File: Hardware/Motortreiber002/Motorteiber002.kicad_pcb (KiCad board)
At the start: 2 copper layers, 159.8 x 99.8 mm, 0 parts

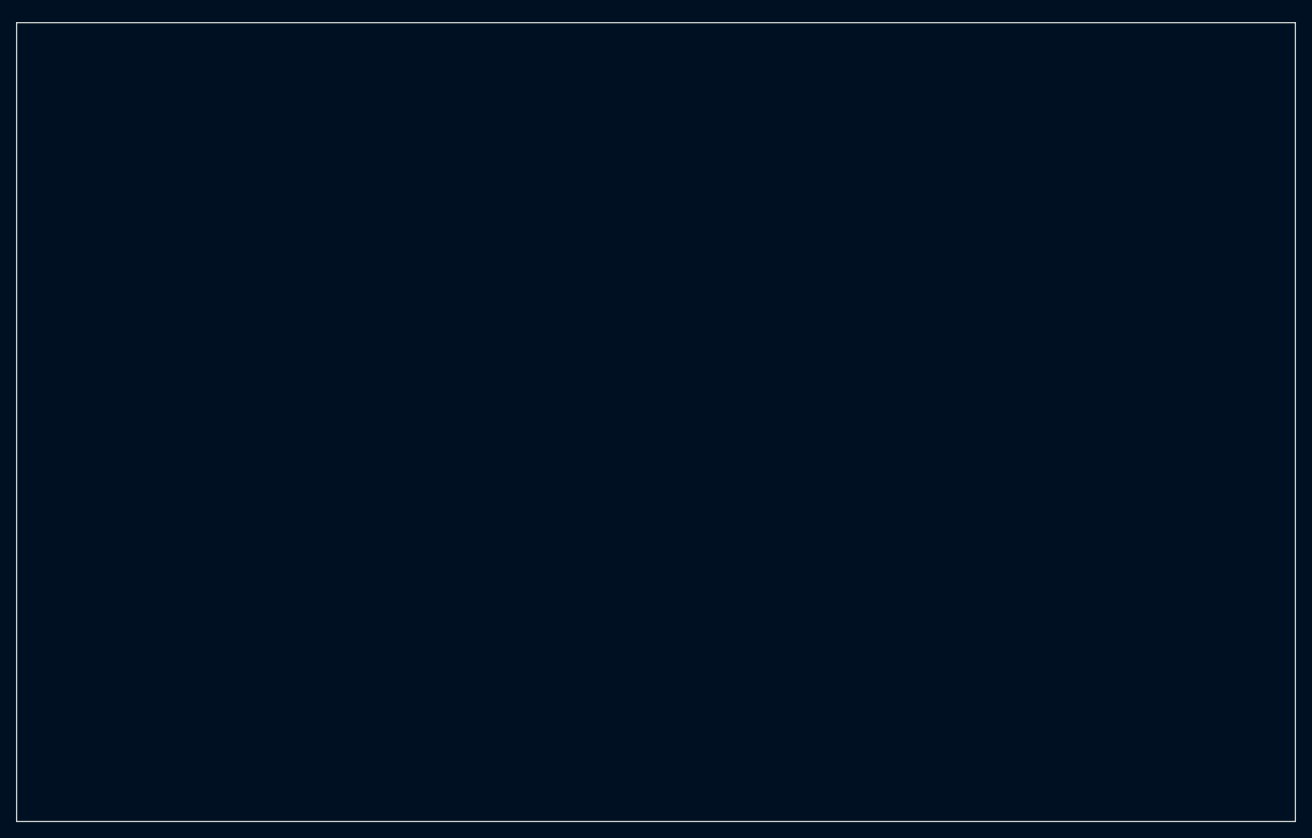
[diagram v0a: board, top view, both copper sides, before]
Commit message: Mega64 hinzu
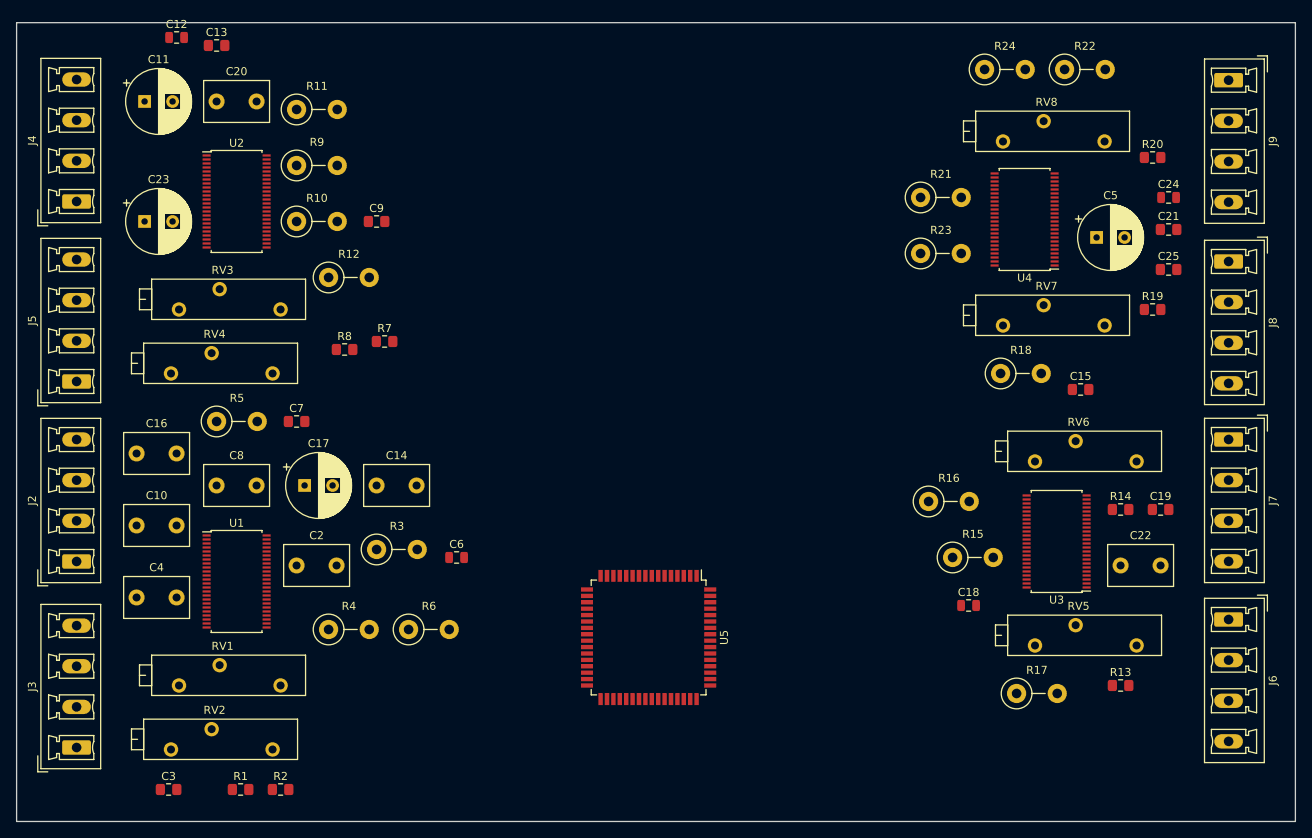
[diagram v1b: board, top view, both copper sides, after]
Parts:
- added C10: 100nF, Capacitor_THT:C_Disc_D8.0mm_W5.0mm_P5.00mm, F.Cu at (70.0, 108.0)
- added C11: 100uF, Capacitor_THT:CP_Radial_D8.0mm_P3.50mm, F.Cu at (71.0, 55.0)
- added C12: 10nF, Capacitor_SMD:C_0805_2012Metric, F.Cu at (75.0, 47.0)
- added C13: 100nf, Capacitor_SMD:C_0805_2012Metric_Pad1.15x1.40mm_HandSolder, F.Cu at (80.0, 48.0)
- added C14: 100nF, Capacitor_THT:C_Disc_D8.0mm_W5.0mm_P5.00mm, F.Cu at (100.0, 103.0)
- added C15: 100nF, Capacitor_SMD:C_0805_2012Metric_Pad1.15x1.40mm_HandSolder, F.Cu at (188.0, 91.0)
- added C16: 100nF, Capacitor_THT:C_Disc_D8.0mm_W5.0mm_P5.00mm, F.Cu at (70.0, 99.0)
- added C17: 100uF, Capacitor_THT:CP_Radial_D8.0mm_P3.50mm, F.Cu at (91.0, 103.0)
- added C18: 10nF, Capacitor_SMD:C_0805_2012Metric, F.Cu at (174.0, 118.0)
- added C19: 100nf, Capacitor_SMD:C_0805_2012Metric_Pad1.15x1.40mm_HandSolder, F.Cu at (198.0, 106.0)
- added C2: 100nF, Capacitor_THT:C_Disc_D8.0mm_W5.0mm_P5.00mm, F.Cu at (90.0, 113.0)
- added C20: 100nF, Capacitor_THT:C_Disc_D8.0mm_W5.0mm_P5.00mm, F.Cu at (80.0, 55.0)
- added C21: 100nF, Capacitor_SMD:C_0805_2012Metric_Pad1.15x1.40mm_HandSolder, F.Cu at (199.0, 71.0)
- added C22: 100nF, Capacitor_THT:C_Disc_D8.0mm_W5.0mm_P5.00mm, F.Cu at (193.0, 113.0)
- added C23: 100uF, Capacitor_THT:CP_Radial_D8.0mm_P3.50mm, F.Cu at (71.0, 70.0)
- added C24: 10nF, Capacitor_SMD:C_0805_2012Metric, F.Cu at (199.0, 67.0)
- added C25: 100nf, Capacitor_SMD:C_0805_2012Metric_Pad1.15x1.40mm_HandSolder, F.Cu at (199.0, 76.0)
- added C3: 100nF, Capacitor_SMD:C_0805_2012Metric_Pad1.15x1.40mm_HandSolder, F.Cu at (74.0, 141.0)
- added C4: 100nF, Capacitor_THT:C_Disc_D8.0mm_W5.0mm_P5.00mm, F.Cu at (70.0, 117.0)
- added C5: 100uF, Capacitor_THT:CP_Radial_D8.0mm_P3.50mm, F.Cu at (190.0, 72.0)
- added C6: 10nF, Capacitor_SMD:C_0805_2012Metric, F.Cu at (110.0, 112.0)
- added C7: 100nf, Capacitor_SMD:C_0805_2012Metric_Pad1.15x1.40mm_HandSolder, F.Cu at (90.0, 95.0)
- added C8: 100nF, Capacitor_THT:C_Disc_D8.0mm_W5.0mm_P5.00mm, F.Cu at (80.0, 103.0)
- added C9: 100nF, Capacitor_SMD:C_0805_2012Metric_Pad1.15x1.40mm_HandSolder, F.Cu at (100.0, 70.0)
- added J2: Screw_Terminal_01x04, Connector_Phoenix_MC_HighVoltage:PhoenixContact_MCV_1,5_4-G-5.08_1x04_P5.08mm_Vertical, F.Cu at (62.5, 112.5)
- added J3: Screw_Terminal_01x04, Connector_Phoenix_MC_HighVoltage:PhoenixContact_MCV_1,5_4-G-5.08_1x04_P5.08mm_Vertical, F.Cu at (62.5, 135.8)
- added J4: Screw_Terminal_01x04, Connector_Phoenix_MC_HighVoltage:PhoenixContact_MCV_1,5_4-G-5.08_1x04_P5.08mm_Vertical, F.Cu at (62.5, 67.5)
- added J5: Screw_Terminal_01x04, Connector_Phoenix_MC_HighVoltage:PhoenixContact_MCV_1,5_4-G-5.08_1x04_P5.08mm_Vertical, F.Cu at (62.5, 90.0)
- added J6: Screw_Terminal_01x04, Connector_Phoenix_MC_HighVoltage:PhoenixContact_MCV_1,5_4-G-5.08_1x04_P5.08mm_Vertical, F.Cu at (206.5, 119.8)
- added J7: Screw_Terminal_01x04, Connector_Phoenix_MC_HighVoltage:PhoenixContact_MCV_1,5_4-G-5.08_1x04_P5.08mm_Vertical, F.Cu at (206.5, 97.2)
- added J8: Screw_Terminal_01x04, Connector_Phoenix_MC_HighVoltage:PhoenixContact_MCV_1,5_4-G-5.08_1x04_P5.08mm_Vertical, F.Cu at (206.5, 75.0)
- added J9: Screw_Terminal_01x04, Connector_Phoenix_MC_HighVoltage:PhoenixContact_MCV_1,5_4-G-5.08_1x04_P5.08mm_Vertical, F.Cu at (206.5, 52.3)
- added R1: R, Resistor_SMD:R_0805_2012Metric_Pad1.15x1.40mm_HandSolder, F.Cu at (83.0, 141.0)
- added R10: 0R5, Resistor_THT:R_Axial_DIN0411_L9.9mm_D3.6mm_P5.08mm_Vertical, F.Cu at (90.0, 70.0)
- added R11: 0R5, Resistor_THT:R_Axial_DIN0411_L9.9mm_D3.6mm_P5.08mm_Vertical, F.Cu at (90.0, 56.0)
- added R12: 0R5, Resistor_THT:R_Axial_DIN0411_L9.9mm_D3.6mm_P5.08mm_Vertical, F.Cu at (94.0, 77.0)
- added R13: R, Resistor_SMD:R_0805_2012Metric_Pad1.15x1.40mm_HandSolder, F.Cu at (193.0, 128.0)
- added R14: R, Resistor_SMD:R_0805_2012Metric_Pad1.15x1.40mm_HandSolder, F.Cu at (193.0, 106.0)
- added R15: 0R5, Resistor_THT:R_Axial_DIN0411_L9.9mm_D3.6mm_P5.08mm_Vertical, F.Cu at (172.0, 112.0)
- added R16: 0R5, Resistor_THT:R_Axial_DIN0411_L9.9mm_D3.6mm_P5.08mm_Vertical, F.Cu at (169.0, 105.0)
- added R17: 0R5, Resistor_THT:R_Axial_DIN0411_L9.9mm_D3.6mm_P5.08mm_Vertical, F.Cu at (180.0, 129.0)
- added R18: 0R5, Resistor_THT:R_Axial_DIN0411_L9.9mm_D3.6mm_P5.08mm_Vertical, F.Cu at (178.0, 89.0)
- added R19: R, Resistor_SMD:R_0805_2012Metric_Pad1.15x1.40mm_HandSolder, F.Cu at (197.0, 81.0)
- added R2: R, Resistor_SMD:R_0805_2012Metric_Pad1.15x1.40mm_HandSolder, F.Cu at (88.0, 141.0)
- added R20: R, Resistor_SMD:R_0805_2012Metric_Pad1.15x1.40mm_HandSolder, F.Cu at (197.0, 62.0)
- added R21: 0R5, Resistor_THT:R_Axial_DIN0411_L9.9mm_D3.6mm_P5.08mm_Vertical, F.Cu at (168.0, 67.0)
- added R22: 0R5, Resistor_THT:R_Axial_DIN0411_L9.9mm_D3.6mm_P5.08mm_Vertical, F.Cu at (186.0, 51.0)
- added R23: 0R5, Resistor_THT:R_Axial_DIN0411_L9.9mm_D3.6mm_P5.08mm_Vertical, F.Cu at (168.0, 74.0)
- added R24: 0R5, Resistor_THT:R_Axial_DIN0411_L9.9mm_D3.6mm_P5.08mm_Vertical, F.Cu at (176.0, 51.0)
- added R3: 0R5, Resistor_THT:R_Axial_DIN0411_L9.9mm_D3.6mm_P5.08mm_Vertical, F.Cu at (100.0, 111.0)
- added R4: 0R5, Resistor_THT:R_Axial_DIN0411_L9.9mm_D3.6mm_P5.08mm_Vertical, F.Cu at (94.0, 121.0)
- added R5: 0R5, Resistor_THT:R_Axial_DIN0411_L9.9mm_D3.6mm_P5.08mm_Vertical, F.Cu at (80.0, 95.0)
- added R6: 0R5, Resistor_THT:R_Axial_DIN0411_L9.9mm_D3.6mm_P5.08mm_Vertical, F.Cu at (104.0, 121.0)
- added R7: R, Resistor_SMD:R_0805_2012Metric_Pad1.15x1.40mm_HandSolder, F.Cu at (101.0, 85.0)
- added R8: R, Resistor_SMD:R_0805_2012Metric_Pad1.15x1.40mm_HandSolder, F.Cu at (96.0, 86.0)
- added R9: 0R5, Resistor_THT:R_Axial_DIN0411_L9.9mm_D3.6mm_P5.08mm_Vertical, F.Cu at (90.0, 63.0)
- added RV1: R_POT_TRIM, Potentiometer_THT:Potentiometer_Vishay_43_Horizontal, F.Cu at (88.0, 128.0)
- added RV2: R_POT_TRIM, Potentiometer_THT:Potentiometer_Vishay_43_Horizontal, F.Cu at (87.0, 136.0)
- added RV3: R_POT_TRIM, Potentiometer_THT:Potentiometer_Vishay_43_Horizontal, F.Cu at (88.0, 81.0)
- added RV4: R_POT_TRIM, Potentiometer_THT:Potentiometer_Vishay_43_Horizontal, F.Cu at (87.0, 89.0)
- added RV5: R_POT_TRIM, Potentiometer_THT:Potentiometer_Vishay_43_Horizontal, F.Cu at (195.0, 123.0)
- added RV6: R_POT_TRIM, Potentiometer_THT:Potentiometer_Vishay_43_Horizontal, F.Cu at (195.0, 100.0)
- added RV7: R_POT_TRIM, Potentiometer_THT:Potentiometer_Vishay_43_Horizontal, F.Cu at (191.0, 83.0)
- added RV8: R_POT_TRIM, Potentiometer_THT:Potentiometer_Vishay_43_Horizontal, F.Cu at (191.0, 60.0)
- added U1: DRV8823, Package_SO:TSSOP-48_6.1x12.5mm_P0.5mm, F.Cu at (82.5, 115.0)
- added U2: DRV8823, Package_SO:TSSOP-48_6.1x12.5mm_P0.5mm, F.Cu at (82.5, 67.5)
- added U3: DRV8823, Package_SO:TSSOP-48_6.1x12.5mm_P0.5mm, F.Cu at (185.0, 110.0)
- added U4: DRV8823, Package_SO:TSSOP-48_6.1x12.5mm_P0.5mm, F.Cu at (181.0, 69.8)
- added U5: ATmega64-16AU, Package_QFP:TQFP-64_14x14mm_P0.8mm, F.Cu at (134.0, 122.0)

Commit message: 16 Motortreiber 1 ATXMega 128 mit USB USB Anschluss noch nicht fertig
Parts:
- removed R1, R13, R14, R19, R2, R20, R7, R8: R, Resistor_SMD:R_0805_2012Metric_Pad1.15x1.40mm_HandSolder
- removed RV1, RV2, RV3, RV4, RV5, RV6, RV7, RV8: R_POT_TRIM, Potentiometer_THT:Potentiometer_Vishay_43_Horizontal
- added C26: 100nF, Capacitor_THT:C_Disc_D8.0mm_W5.0mm_P5.00mm, F.Cu at (179.8, -133.7)
- added C27: 100nF, Capacitor_SMD:C_0805_2012Metric_Pad1.15x1.40mm_HandSolder, F.Cu at (189.4, -135.5)
- added C28: 100nF, Capacitor_THT:C_Disc_D8.0mm_W5.0mm_P5.00mm, F.Cu at (179.5, -127.1)
- added C29: 100uF, Capacitor_THT:CP_Radial_D8.0mm_P3.50mm, F.Cu at (170.7, -128.3)
- added C30: 10nF, Capacitor_SMD:C_0805_2012Metric, F.Cu at (189.4, -145.8)
- added C31: 100nf, Capacitor_SMD:C_0805_2012Metric_Pad1.15x1.40mm_HandSolder, F.Cu at (189.4, -132.5)
- added C32: 100nF, Capacitor_THT:C_Disc_D8.0mm_W5.0mm_P5.00mm, F.Cu at (129.7, -97.8)
- added C33: 100nF, Capacitor_SMD:C_0805_2012Metric_Pad1.15x1.40mm_HandSolder, F.Cu at (139.7, -103.2)
- added C34: 100nF, Capacitor_THT:C_Disc_D8.0mm_W5.0mm_P5.00mm, F.Cu at (130.0, -104.3)
- added C35: 100uF, Capacitor_THT:CP_Radial_D8.0mm_P3.50mm, F.Cu at (120.9, -99.0)
- added C36: 10nF, Capacitor_SMD:C_0805_2012Metric, F.Cu at (139.6, -116.4)
- added C37: 100nf, Capacitor_SMD:C_0805_2012Metric_Pad1.15x1.40mm_HandSolder, F.Cu at (139.7, -106.1)
- added C38: 100nF, Capacitor_THT:C_Disc_D8.0mm_W5.0mm_P5.00mm, F.Cu at (79.9, -68.5)
- added C39: 100nF, Capacitor_SMD:C_0805_2012Metric_Pad1.15x1.40mm_HandSolder, F.Cu at (89.8, -73.8)
- added C40: 100nF, Capacitor_THT:C_Disc_D8.0mm_W5.0mm_P5.00mm, F.Cu at (80.2, -75.0)
- added C41: 100uF, Capacitor_THT:CP_Radial_D8.0mm_P3.50mm, F.Cu at (71.1, -69.7)
- added C42: 10nF, Capacitor_SMD:C_0805_2012Metric, F.Cu at (89.8, -87.1)
- added C43: 100nf, Capacitor_SMD:C_0805_2012Metric_Pad1.15x1.40mm_HandSolder, F.Cu at (89.8, -76.8)
- added C44: 100nF, Capacitor_THT:C_Disc_D8.0mm_W5.0mm_P5.00mm, F.Cu at (30.1, -156.4)
- added C45: 100nF, Capacitor_SMD:C_0805_2012Metric_Pad1.15x1.40mm_HandSolder, F.Cu at (40.0, -164.8)
- added C46: 100nF, Capacitor_THT:C_Disc_D8.0mm_W5.0mm_P5.00mm, F.Cu at (30.4, -163.0)
- added C47: 100uF, Capacitor_THT:CP_Radial_D8.0mm_P3.50mm, F.Cu at (21.3, -157.6)
- added C48: 10nF, Capacitor_SMD:C_0805_2012Metric, F.Cu at (40.0, -175.1)
- added C49: 100nf, Capacitor_SMD:C_0805_2012Metric_Pad1.15x1.40mm_HandSolder, F.Cu at (40.0, -161.8)
- added C50: 100nF, Capacitor_THT:C_Disc_D8.0mm_W5.0mm_P5.00mm, F.Cu at (130.0, -133.7)
- added C51: 100nF, Capacitor_SMD:C_0805_2012Metric_Pad1.15x1.40mm_HandSolder, F.Cu at (139.7, -132.5)
- added C52: 100nF, Capacitor_THT:C_Disc_D8.0mm_W5.0mm_P5.00mm, F.Cu at (129.7, -127.1)
- added C53: 100uF, Capacitor_THT:CP_Radial_D8.0mm_P3.50mm, F.Cu at (120.9, -128.3)
- added C54: 10nF, Capacitor_SMD:C_0805_2012Metric, F.Cu at (139.6, -145.8)
- added C55: 100nf, Capacitor_SMD:C_0805_2012Metric_Pad1.15x1.40mm_HandSolder, F.Cu at (139.7, -135.5)
- added C56: 100nF, Capacitor_THT:C_Disc_D8.0mm_W5.0mm_P5.00mm, F.Cu at (79.9, -97.8)
- added C57: 100nF, Capacitor_SMD:C_0805_2012Metric_Pad1.15x1.40mm_HandSolder, F.Cu at (89.8, -103.2)
- added C58: 100nF, Capacitor_THT:C_Disc_D8.0mm_W5.0mm_P5.00mm, F.Cu at (80.2, -104.3)
- added C59: 100uF, Capacitor_THT:CP_Radial_D8.0mm_P3.50mm, F.Cu at (71.1, -99.0)
- added C60: 10nF, Capacitor_SMD:C_0805_2012Metric, F.Cu at (89.8, -116.4)
- added C61: 100nf, Capacitor_SMD:C_0805_2012Metric_Pad1.15x1.40mm_HandSolder, F.Cu at (89.8, -106.1)
- added C62: 100nF, Capacitor_THT:C_Disc_D8.0mm_W5.0mm_P5.00mm, F.Cu at (30.1, -68.5)
- added C63: 100nF, Capacitor_SMD:C_0805_2012Metric_Pad1.15x1.40mm_HandSolder, F.Cu at (40.0, -73.8)
- added C64: 100nF, Capacitor_THT:C_Disc_D8.0mm_W5.0mm_P5.00mm, F.Cu at (30.4, -75.0)
- added C65: 100uF, Capacitor_THT:CP_Radial_D8.0mm_P3.50mm, F.Cu at (21.3, -69.7)
- added C66: 10nF, Capacitor_SMD:C_0805_2012Metric, F.Cu at (40.0, -87.1)
- added C67: 100nf, Capacitor_SMD:C_0805_2012Metric_Pad1.15x1.40mm_HandSolder, F.Cu at (40.0, -76.8)
- added C68: 100nF, Capacitor_THT:C_Disc_D8.0mm_W5.0mm_P5.00mm, F.Cu at (130.0, -163.0)
- added C69: 100nF, Capacitor_SMD:C_0805_2012Metric_Pad1.15x1.40mm_HandSolder, F.Cu at (139.7, -164.8)
- added C70: 100nF, Capacitor_THT:C_Disc_D8.0mm_W5.0mm_P5.00mm, F.Cu at (129.7, -156.4)
- added C71: 100uF, Capacitor_THT:CP_Radial_D8.0mm_P3.50mm, F.Cu at (120.9, -157.6)
- added C72: 10nF, Capacitor_SMD:C_0805_2012Metric, F.Cu at (139.6, -175.1)
- added C73: 100nf, Capacitor_SMD:C_0805_2012Metric_Pad1.15x1.40mm_HandSolder, F.Cu at (139.7, -161.8)
- added C74: 100nF, Capacitor_THT:C_Disc_D8.0mm_W5.0mm_P5.00mm, F.Cu at (80.2, -133.7)
- added C75: 100nF, Capacitor_SMD:C_0805_2012Metric_Pad1.15x1.40mm_HandSolder, F.Cu at (89.8, -132.5)
- added C76: 100nF, Capacitor_THT:C_Disc_D8.0mm_W5.0mm_P5.00mm, F.Cu at (79.9, -127.1)
- added C77: 100uF, Capacitor_THT:CP_Radial_D8.0mm_P3.50mm, F.Cu at (71.1, -128.3)
- added C78: 10nF, Capacitor_SMD:C_0805_2012Metric, F.Cu at (89.8, -145.8)
- added C79: 100nf, Capacitor_SMD:C_0805_2012Metric_Pad1.15x1.40mm_HandSolder, F.Cu at (89.8, -135.5)
- added C80: 100nF, Capacitor_THT:C_Disc_D8.0mm_W5.0mm_P5.00mm, F.Cu at (30.4, -104.3)
- added C81: 100nF, Capacitor_SMD:C_0805_2012Metric_Pad1.15x1.40mm_HandSolder, F.Cu at (40.0, -106.1)
- added C82: 100nF, Capacitor_THT:C_Disc_D8.0mm_W5.0mm_P5.00mm, F.Cu at (30.1, -97.8)
- added C83: 100uF, Capacitor_THT:CP_Radial_D8.0mm_P3.50mm, F.Cu at (21.3, -99.0)
- added C84: 10nF, Capacitor_SMD:C_0805_2012Metric, F.Cu at (40.0, -116.4)
- added C85: 100nf, Capacitor_SMD:C_0805_2012Metric_Pad1.15x1.40mm_HandSolder, F.Cu at (40.0, -103.2)
- added C86: 100nF, Capacitor_THT:C_Disc_D8.0mm_W5.0mm_P5.00mm, F.Cu at (79.9, -156.4)
- added C87: 100nF, Capacitor_SMD:C_0805_2012Metric_Pad1.15x1.40mm_HandSolder, F.Cu at (89.8, -161.8)
- added C88: 100nF, Capacitor_THT:C_Disc_D8.0mm_W5.0mm_P5.00mm, F.Cu at (80.2, -163.0)
- added C89: 100uF, Capacitor_THT:CP_Radial_D8.0mm_P3.50mm, F.Cu at (71.1, -157.6)
- added C90: 10nF, Capacitor_SMD:C_0805_2012Metric, F.Cu at (89.8, -175.1)
- added C91: 100nf, Capacitor_SMD:C_0805_2012Metric_Pad1.15x1.40mm_HandSolder, F.Cu at (89.8, -164.8)
- added C92: 100nF, Capacitor_THT:C_Disc_D8.0mm_W5.0mm_P5.00mm, F.Cu at (30.4, -133.7)
- added C93: 100nF, Capacitor_SMD:C_0805_2012Metric_Pad1.15x1.40mm_HandSolder, F.Cu at (40.0, -135.5)
- added C94: 100nF, Capacitor_THT:C_Disc_D8.0mm_W5.0mm_P5.00mm, F.Cu at (30.1, -127.1)
- added C95: 100uF, Capacitor_THT:CP_Radial_D8.0mm_P3.50mm, F.Cu at (21.3, -128.3)
- added C96: 10nF, Capacitor_SMD:C_0805_2012Metric, F.Cu at (40.0, -145.8)
- added C97: 100nf, Capacitor_SMD:C_0805_2012Metric_Pad1.15x1.40mm_HandSolder, F.Cu at (40.0, -132.5)
- added J10: Screw_Terminal_01x04, Connector_Phoenix_MC_HighVoltage:PhoenixContact_MCV_1,5_4-G-5.08_1x04_P5.08mm_Vertical, F.Cu at (148.7, -141.8)
- added J11: Screw_Terminal_01x04, Connector_Phoenix_MC_HighVoltage:PhoenixContact_MCV_1,5_4-G-5.08_1x04_P5.08mm_Vertical, F.Cu at (148.7, -132.5)
- added J12: Screw_Terminal_01x04, Connector_Phoenix_MC_HighVoltage:PhoenixContact_MCV_1,5_4-G-5.08_1x04_P5.08mm_Vertical, F.Cu at (98.9, -112.5)
- added J13: Screw_Terminal_01x04, Connector_Phoenix_MC_HighVoltage:PhoenixContact_MCV_1,5_4-G-5.08_1x04_P5.08mm_Vertical, F.Cu at (98.9, -103.2)
- added J14: Screw_Terminal_01x04, Connector_Phoenix_MC_HighVoltage:PhoenixContact_MCV_1,5_4-G-5.08_1x04_P5.08mm_Vertical, F.Cu at (49.1, -83.2)
- added J15: Screw_Terminal_01x04, Connector_Phoenix_MC_HighVoltage:PhoenixContact_MCV_1,5_4-G-5.08_1x04_P5.08mm_Vertical, F.Cu at (49.1, -73.8)
- added J16: Screw_Terminal_01x04, Connector_Phoenix_MC_HighVoltage:PhoenixContact_MCV_1,5_4-G-5.08_1x04_P5.08mm_Vertical, F.Cu at (-0.72, -171.2)
- added J17: Screw_Terminal_01x04, Connector_Phoenix_MC_HighVoltage:PhoenixContact_MCV_1,5_4-G-5.08_1x04_P5.08mm_Vertical, F.Cu at (-0.72, -161.8)
- added J18: Screw_Terminal_01x04, Connector_Phoenix_MC_HighVoltage:PhoenixContact_MCV_1,5_4-G-5.08_1x04_P5.08mm_Vertical, F.Cu at (98.9, -132.5)
- added J19: Screw_Terminal_01x04, Connector_Phoenix_MC_HighVoltage:PhoenixContact_MCV_1,5_4-G-5.08_1x04_P5.08mm_Vertical, F.Cu at (98.9, -141.8)
- added J20: Screw_Terminal_01x04, Connector_Phoenix_MC_HighVoltage:PhoenixContact_MCV_1,5_4-G-5.08_1x04_P5.08mm_Vertical, F.Cu at (49.1, -112.5)
- added J21: Screw_Terminal_01x04, Connector_Phoenix_MC_HighVoltage:PhoenixContact_MCV_1,5_4-G-5.08_1x04_P5.08mm_Vertical, F.Cu at (49.1, -103.2)
- added J22: Screw_Terminal_01x04, Connector_Phoenix_MC_HighVoltage:PhoenixContact_MCV_1,5_4-G-5.08_1x04_P5.08mm_Vertical, F.Cu at (-0.72, -73.8)
- added J23: Screw_Terminal_01x04, Connector_Phoenix_MC_HighVoltage:PhoenixContact_MCV_1,5_4-G-5.08_1x04_P5.08mm_Vertical, F.Cu at (-0.72, -83.2)
- added J24: Screw_Terminal_01x04, Connector_Phoenix_MC_HighVoltage:PhoenixContact_MCV_1,5_4-G-5.08_1x04_P5.08mm_Vertical, F.Cu at (98.9, -171.2)
- added J25: Screw_Terminal_01x04, Connector_Phoenix_MC_HighVoltage:PhoenixContact_MCV_1,5_4-G-5.08_1x04_P5.08mm_Vertical, F.Cu at (98.9, -161.8)
- added J26: Screw_Terminal_01x04, Connector_Phoenix_MC_HighVoltage:PhoenixContact_MCV_1,5_4-G-5.08_1x04_P5.08mm_Vertical, F.Cu at (49.1, -132.5)
- added J27: Screw_Terminal_01x04, Connector_Phoenix_MC_HighVoltage:PhoenixContact_MCV_1,5_4-G-5.08_1x04_P5.08mm_Vertical, F.Cu at (49.1, -141.8)
- added J28: Screw_Terminal_01x04, Connector_Phoenix_MC_HighVoltage:PhoenixContact_MCV_1,5_4-G-5.08_1x04_P5.08mm_Vertical, F.Cu at (-0.72, -103.2)
- added J29: Screw_Terminal_01x04, Connector_Phoenix_MC_HighVoltage:PhoenixContact_MCV_1,5_4-G-5.08_1x04_P5.08mm_Vertical, F.Cu at (-0.72, -112.5)
- added J30: Screw_Terminal_01x04, Connector_Phoenix_MC_HighVoltage:PhoenixContact_MCV_1,5_4-G-5.08_1x04_P5.08mm_Vertical, F.Cu at (49.1, -161.8)
- added J31: Screw_Terminal_01x04, Connector_Phoenix_MC_HighVoltage:PhoenixContact_MCV_1,5_4-G-5.08_1x04_P5.08mm_Vertical, F.Cu at (49.1, -171.2)
- added J32: Screw_Terminal_01x04, Connector_Phoenix_MC_HighVoltage:PhoenixContact_MCV_1,5_4-G-5.08_1x04_P5.08mm_Vertical, F.Cu at (-0.72, -132.5)
- added J33: Screw_Terminal_01x04, Connector_Phoenix_MC_HighVoltage:PhoenixContact_MCV_1,5_4-G-5.08_1x04_P5.08mm_Vertical, F.Cu at (-0.72, -141.8)
- added R27: 0R5, Resistor_THT:R_Axial_DIN0411_L9.9mm_D3.6mm_P5.08mm_Vertical, F.Cu at (147.7, -126.0)
- added R28: 0R5, Resistor_THT:R_Axial_DIN0411_L9.9mm_D3.6mm_P5.08mm_Vertical, F.Cu at (180.1, -139.5)
- added R29: 0R5, Resistor_THT:R_Axial_DIN0411_L9.9mm_D3.6mm_P5.08mm_Vertical, F.Cu at (180.1, -144.7)
- added R30: 0R5, Resistor_THT:R_Axial_DIN0411_L9.9mm_D3.6mm_P5.08mm_Vertical, F.Cu at (157.3, -126.0)
- added R33: 0R5, Resistor_THT:R_Axial_DIN0411_L9.9mm_D3.6mm_P5.08mm_Vertical, F.Cu at (130.3, -110.2)
- added R34: 0R5, Resistor_THT:R_Axial_DIN0411_L9.9mm_D3.6mm_P5.08mm_Vertical, F.Cu at (130.3, -115.3)
- added R35: 0R5, Resistor_THT:R_Axial_DIN0411_L9.9mm_D3.6mm_P5.08mm_Vertical, F.Cu at (97.8, -96.7)
- added R36: 0R5, Resistor_THT:R_Axial_DIN0411_L9.9mm_D3.6mm_P5.08mm_Vertical, F.Cu at (107.5, -96.7)
- added R39: 0R5, Resistor_THT:R_Axial_DIN0411_L9.9mm_D3.6mm_P5.08mm_Vertical, F.Cu at (57.7, -67.3)
- added R40: 0R5, Resistor_THT:R_Axial_DIN0411_L9.9mm_D3.6mm_P5.08mm_Vertical, F.Cu at (48.0, -67.3)
- added R41: 0R5, Resistor_THT:R_Axial_DIN0411_L9.9mm_D3.6mm_P5.08mm_Vertical, F.Cu at (80.5, -86.0)
- added R42: 0R5, Resistor_THT:R_Axial_DIN0411_L9.9mm_D3.6mm_P5.08mm_Vertical, F.Cu at (80.5, -80.8)
- added R45: 0R5, Resistor_THT:R_Axial_DIN0411_L9.9mm_D3.6mm_P5.08mm_Vertical, F.Cu at (30.7, -168.8)
- added R46: 0R5, Resistor_THT:R_Axial_DIN0411_L9.9mm_D3.6mm_P5.08mm_Vertical, F.Cu at (30.7, -174.0)
- added R47: 0R5, Resistor_THT:R_Axial_DIN0411_L9.9mm_D3.6mm_P5.08mm_Vertical, F.Cu at (7.88, -155.3)
- added R48: 0R5, Resistor_THT:R_Axial_DIN0411_L9.9mm_D3.6mm_P5.08mm_Vertical, F.Cu at (-1.75, -155.3)
- added R51: 0R5, Resistor_THT:R_Axial_DIN0411_L9.9mm_D3.6mm_P5.08mm_Vertical, F.Cu at (130.3, -139.5)
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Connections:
- J2 pad 1: /Motortreiber1/MA1 -> /Motortreiber4/MA1
- J2 pad 2: /Motortreiber1/MA2 -> /Motortreiber4/MA2
- J2 pad 3: /Motortreiber1/MB2 -> /Motortreiber4/MB2
- J2 pad 4: /Motortreiber1/MB1 -> /Motortreiber4/MB1
- J3 pad 1: /Motortreiber1/MC1 -> /Motortreiber4/MC1
- J3 pad 2: /Motortreiber1/MC2 -> /Motortreiber4/MC2
- J3 pad 3: /Motortreiber1/MD1 -> /Motortreiber4/MD1
- J3 pad 4: /Motortreiber1/MD2 -> /Motortreiber4/MD2
- J4 pad 1: /Motortreiber2/MA1 -> /Motortreiber5/MA1
- J4 pad 2: /Motortreiber2/MA2 -> /Motortreiber5/MA2
- J4 pad 3: /Motortreiber2/MB2 -> /Motortreiber5/MB2
- J4 pad 4: /Motortreiber2/MB1 -> /Motortreiber5/MB1
- J5 pad 1: /Motortreiber2/MC1 -> /Motortreiber5/MC1
- J5 pad 2: /Motortreiber2/MC2 -> /Motortreiber5/MC2
- J5 pad 3: /Motortreiber2/MD1 -> /Motortreiber5/MD1
- J5 pad 4: /Motortreiber2/MD2 -> /Motortreiber5/MD2
- J8 pad 1: /Motortreiber4/MA1 -> /Motortreiber2/MA1
- J8 pad 2: /Motortreiber4/MA2 -> /Motortreiber2/MA2
- J8 pad 3: /Motortreiber4/MB2 -> /Motortreiber2/MB2
- J8 pad 4: /Motortreiber4/MB1 -> /Motortreiber2/MB1
- J9 pad 1: /Motortreiber4/MC1 -> /Motortreiber2/MC1
- J9 pad 2: /Motortreiber4/MC2 -> /Motortreiber2/MC2
- J9 pad 3: /Motortreiber4/MD1 -> /Motortreiber2/MD1
- J9 pad 4: /Motortreiber4/MD2 -> /Motortreiber2/MD2
- U1 pad 17: Net-(RV1-Pad2) -> /Motortreiber4/ABVRef
- U1 pad 18: Net-(RV2-Pad2) -> /Motortreiber4/CDVRef
- U1 pad 20: /Motortreiber1/MD2 -> /Motortreiber4/MD2
- U1 pad 22: /Motortreiber1/MD1 -> /Motortreiber4/MD1
- U1 pad 25: /Motortreiber1/MC2 -> /Motortreiber4/MC2
- U1 pad 27: /Motortreiber1/MC1 -> /Motortreiber4/MC1
- U1 pad 3: /Motortreiber1/MA2 -> /Motortreiber4/MA2
- U1 pad 30: /Ue1 -> /Strobe4
- U1 pad 45: /CS1 -> /CS
- U1 pad 46: /Motortreiber1/MB1 -> /Motortreiber4/MB1
- U1 pad 48: /Motortreiber1/MB2 -> /Motortreiber4/MB2
- U1 pad 5: /Motortreiber1/MA1 -> /Motortreiber4/MA1
- U2 pad 17: Net-(RV3-Pad2) -> /Motortreiber5/ABVRef
- U2 pad 18: Net-(RV4-Pad2) -> /Motortreiber5/CDVRef
- U2 pad 20: /Motortreiber2/MD2 -> /Motortreiber5/MD2
- U2 pad 22: /Motortreiber2/MD1 -> /Motortreiber5/MD1
- U2 pad 25: /Motortreiber2/MC2 -> /Motortreiber5/MC2
- U2 pad 27: /Motortreiber2/MC1 -> /Motortreiber5/MC1
- U2 pad 3: /Motortreiber2/MA2 -> /Motortreiber5/MA2
- U2 pad 30: /Ue2 -> /Strobe5
- U2 pad 45: /CS2 -> /CS
- U2 pad 46: /Motortreiber2/MB1 -> /Motortreiber5/MB1
- U2 pad 48: /Motortreiber2/MB2 -> /Motortreiber5/MB2
- U2 pad 5: /Motortreiber2/MA1 -> /Motortreiber5/MA1
- U3 pad 17: Net-(RV5-Pad2) -> /Motortreiber3/ABVRef
- U3 pad 18: Net-(RV6-Pad2) -> /Motortreiber3/CDVRef
- U3 pad 30: /Ue3 -> /Strobe3
- U3 pad 45: /CS3 -> /CS
- U4 pad 17: Net-(RV7-Pad2) -> /Motortreiber2/ABVRef
- U4 pad 18: Net-(RV8-Pad2) -> /Motortreiber2/CDVRef
- U4 pad 20: /Motortreiber4/MD2 -> /Motortreiber2/MD2
- U4 pad 22: /Motortreiber4/MD1 -> /Motortreiber2/MD1
- U4 pad 25: /Motortreiber4/MC2 -> /Motortreiber2/MC2
- U4 pad 27: /Motortreiber4/MC1 -> /Motortreiber2/MC1
- U4 pad 3: /Motortreiber4/MA2 -> /Motortreiber2/MA2
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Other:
- board size 159.8 x 99.8 mm -> 210 x 290 mm

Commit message: Annotation auf Seiten bezogen
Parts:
- removed C10, C14, C16, C2, C20, C22, C26, C28, C32, C34, C38, C4, C40, C44, C46, C50, C52, C56, C58, C62, C64, C68, C70, C74, C76, C8, C80, C82, C86, C88, C92, C94: 100nF, Capacitor_THT:C_Disc_D8.0mm_W5.0mm_P5.00mm
- removed C11, C17, C23, C29, C35, C41, C47, C5, C53, C59, C65, C71, C77, C83, C89, C95: 100uF, Capacitor_THT:CP_Radial_D8.0mm_P3.50mm
- removed C12, C18, C24, C30, C36, C42, C48, C54, C6, C60, C66, C72, C78, C84, C90, C96: 10nF, Capacitor_SMD:C_0805_2012Metric
- removed C13, C19, C25, C31, C37, C43, C49, C55, C61, C67, C7, C73, C79, C85, C91, C97: 100nf, Capacitor_SMD:C_0805_2012Metric_Pad1.15x1.40mm_HandSolder
- removed C15, C21, C27, C3, C33, C39, C45, C51, C57, C63, C69, C75, C81, C87, C9, C93: 100nF, Capacitor_SMD:C_0805_2012Metric_Pad1.15x1.40mm_HandSolder
- removed J10, J11, J12, J13, J14, J15, J16, J17, J18, J19, J2, J20, J21, J22, J23, J24, J25, J26, J27, J28, J29, J3, J30, J31, J32, J33, J4, J5, J6, J7, J8, J9: Screw_Terminal_01x04, Connector_Phoenix_MC_HighVoltage:PhoenixContact_MCV_1,5_4-G-5.08_1x04_P5.08mm_Vertical
- removed R10, R11, R12, R15, R16, R17, R18, R21, R22, R23, R24, R27, R28, R29, R3, R30, R33, R34, R35, R36, R39, R4, R40, R41, R42, R45, R46, R47, R48, R5, R51, R52, R53, R54, R57, R58, R59, R6, R60, R63, R64, R65, R66, R69, R70, R71, R72, R75, R76, R77, R78, R81, R82, R83, R84, R87, R88, R89, R9, R90, R93, R94, R95, R96: 0R5, Resistor_THT:R_Axial_DIN0411_L9.9mm_D3.6mm_P5.08mm_Vertical
- removed U1, U10, U11, U12, U13, U14, U15, U16, U17, U18, U2, U3, U4, U7, U8, U9: DRV8823, Package_SO:TSSOP-48_6.1x12.5mm_P0.5mm
- removed U5: ADUM3160, Package_SO:SOIC-16W_7.5x10.3mm_P1.27mm
- removed U6: ATxmega128C3-AU, Package_QFP:TQFP-64_14x14mm_P0.8mm
- added C1001: 100nF, Capacitor_THT:C_Disc_D8.0mm_W5.0mm_P5.00mm, F.Cu at (85.6, -125.7)
- added C1002: 100nF, Capacitor_SMD:C_0805_2012Metric_Pad1.15x1.40mm_HandSolder, F.Cu at (95.6, -131.1)
- added C1003: 100nF, Capacitor_THT:C_Disc_D8.0mm_W5.0mm_P5.00mm, F.Cu at (85.9, -132.2)
- added C1005: 100uF, Capacitor_THT:CP_Radial_D8.0mm_P3.50mm, F.Cu at (76.8, -126.9)
- added C1007: 10nF, Capacitor_SMD:C_0805_2012Metric, F.Cu at (95.5, -144.3)
- added C1008: 100nf, Capacitor_SMD:C_0805_2012Metric_Pad1.15x1.40mm_HandSolder, F.Cu at (95.6, -134.0)
- added C1101: 100nF, Capacitor_THT:C_Disc_D8.0mm_W5.0mm_P5.00mm, F.Cu at (85.9, -161.6)
- added C1102: 100nF, Capacitor_SMD:C_0805_2012Metric_Pad1.15x1.40mm_HandSolder, F.Cu at (95.6, -163.3)
- added C1103: 100nF, Capacitor_THT:C_Disc_D8.0mm_W5.0mm_P5.00mm, F.Cu at (85.6, -155.0)
- added C1105: 100uF, Capacitor_THT:CP_Radial_D8.0mm_P3.50mm, F.Cu at (76.8, -156.2)
- added C1107: 10nF, Capacitor_SMD:C_0805_2012Metric, F.Cu at (95.5, -173.7)
- added C1108: 100nf, Capacitor_SMD:C_0805_2012Metric_Pad1.15x1.40mm_HandSolder, F.Cu at (95.6, -160.4)
- added C1201: 100nF, Capacitor_THT:C_Disc_D8.0mm_W5.0mm_P5.00mm, F.Cu at (36.1, -132.2)
- added C1202: 100nF, Capacitor_SMD:C_0805_2012Metric_Pad1.15x1.40mm_HandSolder, F.Cu at (45.8, -134.0)
- added C1203: 100nF, Capacitor_THT:C_Disc_D8.0mm_W5.0mm_P5.00mm, F.Cu at (35.8, -125.7)
- added C1205: 100uF, Capacitor_THT:CP_Radial_D8.0mm_P3.50mm, F.Cu at (27.0, -126.9)
- added C1207: 10nF, Capacitor_SMD:C_0805_2012Metric, F.Cu at (45.7, -144.3)
- added C1208: 100nf, Capacitor_SMD:C_0805_2012Metric_Pad1.15x1.40mm_HandSolder, F.Cu at (45.8, -131.1)
- added C1301: 100nF, Capacitor_THT:C_Disc_D8.0mm_W5.0mm_P5.00mm, F.Cu at (185.2, -155.0)
- added C1302: 100nF, Capacitor_SMD:C_0805_2012Metric_Pad1.15x1.40mm_HandSolder, F.Cu at (195.2, -160.4)
- added C1303: 100nF, Capacitor_THT:C_Disc_D8.0mm_W5.0mm_P5.00mm, F.Cu at (185.5, -161.6)
- added C1305: 100uF, Capacitor_THT:CP_Radial_D8.0mm_P3.50mm, F.Cu at (176.4, -156.2)
- added C1307: 10nF, Capacitor_SMD:C_0805_2012Metric, F.Cu at (195.1, -173.7)
- added C1308: 100nf, Capacitor_SMD:C_0805_2012Metric_Pad1.15x1.40mm_HandSolder, F.Cu at (195.2, -163.3)
- added C1401: 100nF, Capacitor_THT:C_Disc_D8.0mm_W5.0mm_P5.00mm, F.Cu at (36.1, -73.6)
- added C1402: 100nF, Capacitor_SMD:C_0805_2012Metric_Pad1.15x1.40mm_HandSolder, F.Cu at (45.8, -75.4)
- added C1403: 100nF, Capacitor_THT:C_Disc_D8.0mm_W5.0mm_P5.00mm, F.Cu at (35.8, -67.0)
- added C1405: 100uF, Capacitor_THT:CP_Radial_D8.0mm_P3.50mm, F.Cu at (27.0, -68.2)
- added C1407: 10nF, Capacitor_SMD:C_0805_2012Metric, F.Cu at (45.7, -85.7)
- added C1408: 100nf, Capacitor_SMD:C_0805_2012Metric_Pad1.15x1.40mm_HandSolder, F.Cu at (45.8, -72.4)
- added C1501: 100nF, Capacitor_THT:C_Disc_D8.0mm_W5.0mm_P5.00mm, F.Cu at (85.9, -102.9)
- added C1502: 100nF, Capacitor_SMD:C_0805_2012Metric_Pad1.15x1.40mm_HandSolder, F.Cu at (95.6, -104.7)
- added C1503: 100nF, Capacitor_THT:C_Disc_D8.0mm_W5.0mm_P5.00mm, F.Cu at (85.6, -96.3)
- added C1505: 100uF, Capacitor_THT:CP_Radial_D8.0mm_P3.50mm, F.Cu at (76.8, -97.5)
- added C1507: 10nF, Capacitor_SMD:C_0805_2012Metric, F.Cu at (95.5, -115.0)
- added C1508: 100nf, Capacitor_SMD:C_0805_2012Metric_Pad1.15x1.40mm_HandSolder, F.Cu at (95.6, -101.7)
- added C1601: 100nF, Capacitor_THT:C_Disc_D8.0mm_W5.0mm_P5.00mm, F.Cu at (135.4, -67.0)
- added C1602: 100nF, Capacitor_SMD:C_0805_2012Metric_Pad1.15x1.40mm_HandSolder, F.Cu at (145.4, -72.4)
- added C1603: 100nF, Capacitor_THT:C_Disc_D8.0mm_W5.0mm_P5.00mm, F.Cu at (135.7, -73.6)
- added C1605: 100uF, Capacitor_THT:CP_Radial_D8.0mm_P3.50mm, F.Cu at (126.6, -68.2)
- added C1607: 10nF, Capacitor_SMD:C_0805_2012Metric, F.Cu at (145.3, -85.7)
- added C1608: 100nf, Capacitor_SMD:C_0805_2012Metric_Pad1.15x1.40mm_HandSolder, F.Cu at (145.4, -75.4)
- added C1701: 100nF, Capacitor_THT:C_Disc_D8.0mm_W5.0mm_P5.00mm, F.Cu at (36.1, -161.6)
- added C1702: 100nF, Capacitor_SMD:C_0805_2012Metric_Pad1.15x1.40mm_HandSolder, F.Cu at (45.8, -163.3)
- added C1703: 100nF, Capacitor_THT:C_Disc_D8.0mm_W5.0mm_P5.00mm, F.Cu at (35.8, -155.0)
- added C1705: 100uF, Capacitor_THT:CP_Radial_D8.0mm_P3.50mm, F.Cu at (27.0, -156.2)
- added C1707: 10nF, Capacitor_SMD:C_0805_2012Metric, F.Cu at (45.7, -173.7)
- added C1708: 100nf, Capacitor_SMD:C_0805_2012Metric_Pad1.15x1.40mm_HandSolder, F.Cu at (45.8, -160.4)
- added C1801: 100nF, Capacitor_THT:C_Disc_D8.0mm_W5.0mm_P5.00mm, F.Cu at (36.1, -102.9)
- added C1802: 100nF, Capacitor_SMD:C_0805_2012Metric_Pad1.15x1.40mm_HandSolder, F.Cu at (45.8, -104.7)
- added C1803: 100nF, Capacitor_THT:C_Disc_D8.0mm_W5.0mm_P5.00mm, F.Cu at (35.8, -96.3)
- added C1805: 100uF, Capacitor_THT:CP_Radial_D8.0mm_P3.50mm, F.Cu at (27.0, -97.5)
- added C1807: 10nF, Capacitor_SMD:C_0805_2012Metric, F.Cu at (45.7, -115.0)
- added C1808: 100nf, Capacitor_SMD:C_0805_2012Metric_Pad1.15x1.40mm_HandSolder, F.Cu at (45.8, -101.7)
- added C1901: 100nF, Capacitor_THT:C_Disc_D8.0mm_W5.0mm_P5.00mm, F.Cu at (85.6, -67.0)
- added C1902: 100nF, Capacitor_SMD:C_0805_2012Metric_Pad1.15x1.40mm_HandSolder, F.Cu at (95.6, -72.4)
- added C1903: 100nF, Capacitor_THT:C_Disc_D8.0mm_W5.0mm_P5.00mm, F.Cu at (85.9, -73.6)
- added C1905: 100uF, Capacitor_THT:CP_Radial_D8.0mm_P3.50mm, F.Cu at (76.8, -68.2)
- added C1907: 10nF, Capacitor_SMD:C_0805_2012Metric, F.Cu at (95.5, -85.7)
- added C1908: 100nf, Capacitor_SMD:C_0805_2012Metric_Pad1.15x1.40mm_HandSolder, F.Cu at (95.6, -75.4)
- added C301: 100nF, Capacitor_THT:C_Disc_D8.0mm_W5.0mm_P5.00mm, F.Cu at (235.0, -155.0)
- added C302: 100nF, Capacitor_SMD:C_0805_2012Metric_Pad1.15x1.40mm_HandSolder, F.Cu at (245.0, -163.3)
- added C303: 100nF, Capacitor_THT:C_Disc_D8.0mm_W5.0mm_P5.00mm, F.Cu at (235.3, -161.6)
- added C305: 100uF, Capacitor_THT:CP_Radial_D8.0mm_P3.50mm, F.Cu at (226.2, -156.2)
- added C307: 10nF, Capacitor_SMD:C_0805_2012Metric, F.Cu at (244.9, -173.7)
- added C308: 100nf, Capacitor_SMD:C_0805_2012Metric_Pad1.15x1.40mm_HandSolder, F.Cu at (245.0, -160.4)
- added C401: 100nF, Capacitor_THT:C_Disc_D8.0mm_W5.0mm_P5.00mm, F.Cu at (185.2, -96.3)
- added C402: 100nF, Capacitor_SMD:C_0805_2012Metric_Pad1.15x1.40mm_HandSolder, F.Cu at (195.2, -101.7)
- added C403: 100nF, Capacitor_THT:C_Disc_D8.0mm_W5.0mm_P5.00mm, F.Cu at (185.5, -102.9)
- added C405: 100uF, Capacitor_THT:CP_Radial_D8.0mm_P3.50mm, F.Cu at (176.4, -97.5)
- added C407: 10nF, Capacitor_SMD:C_0805_2012Metric, F.Cu at (195.1, -115.0)
- added C408: 100nf, Capacitor_SMD:C_0805_2012Metric_Pad1.15x1.40mm_HandSolder, F.Cu at (195.2, -104.7)
- added C601: 100nF, Capacitor_THT:C_Disc_D8.0mm_W5.0mm_P5.00mm, F.Cu at (185.5, -132.2)
- added C602: 100nF, Capacitor_SMD:C_0805_2012Metric_Pad1.15x1.40mm_HandSolder, F.Cu at (195.2, -134.0)
- added C603: 100nF, Capacitor_THT:C_Disc_D8.0mm_W5.0mm_P5.00mm, F.Cu at (185.2, -125.7)
- added C605: 100uF, Capacitor_THT:CP_Radial_D8.0mm_P3.50mm, F.Cu at (176.4, -126.9)
- added C607: 10nF, Capacitor_SMD:C_0805_2012Metric, F.Cu at (195.1, -144.3)
- added C608: 100nf, Capacitor_SMD:C_0805_2012Metric_Pad1.15x1.40mm_HandSolder, F.Cu at (195.2, -131.1)
- added C701: 100nF, Capacitor_THT:C_Disc_D8.0mm_W5.0mm_P5.00mm, F.Cu at (135.7, -102.9)
- added C702: 100nF, Capacitor_SMD:C_0805_2012Metric_Pad1.15x1.40mm_HandSolder, F.Cu at (145.4, -104.7)
- added C703: 100nF, Capacitor_THT:C_Disc_D8.0mm_W5.0mm_P5.00mm, F.Cu at (135.4, -96.3)
- added C705: 100uF, Capacitor_THT:CP_Radial_D8.0mm_P3.50mm, F.Cu at (126.6, -97.5)
- added C707: 10nF, Capacitor_SMD:C_0805_2012Metric, F.Cu at (145.3, -115.0)
- added C708: 100nf, Capacitor_SMD:C_0805_2012Metric_Pad1.15x1.40mm_HandSolder, F.Cu at (145.4, -101.7)
- added C801: 100nF, Capacitor_THT:C_Disc_D8.0mm_W5.0mm_P5.00mm, F.Cu at (135.4, -125.7)
- added C802: 100nF, Capacitor_SMD:C_0805_2012Metric_Pad1.15x1.40mm_HandSolder, F.Cu at (145.4, -131.1)
- added C803: 100nF, Capacitor_THT:C_Disc_D8.0mm_W5.0mm_P5.00mm, F.Cu at (135.7, -132.2)
- added C805: 100uF, Capacitor_THT:CP_Radial_D8.0mm_P3.50mm, F.Cu at (126.6, -126.9)
- added C807: 10nF, Capacitor_SMD:C_0805_2012Metric, F.Cu at (145.3, -144.3)
- added C808: 100nf, Capacitor_SMD:C_0805_2012Metric_Pad1.15x1.40mm_HandSolder, F.Cu at (145.4, -134.0)
- added C901: 100nF, Capacitor_THT:C_Disc_D8.0mm_W5.0mm_P5.00mm, F.Cu at (135.4, -155.0)
- added C902: 100nF, Capacitor_SMD:C_0805_2012Metric_Pad1.15x1.40mm_HandSolder, F.Cu at (145.4, -160.4)
- added C903: 100nF, Capacitor_THT:C_Disc_D8.0mm_W5.0mm_P5.00mm, F.Cu at (135.7, -161.6)
- added C905: 100uF, Capacitor_THT:CP_Radial_D8.0mm_P3.50mm, F.Cu at (126.6, -156.2)
- added C907: 10nF, Capacitor_SMD:C_0805_2012Metric, F.Cu at (145.3, -173.7)
- added C908: 100nf, Capacitor_SMD:C_0805_2012Metric_Pad1.15x1.40mm_HandSolder, F.Cu at (145.4, -163.3)
- added J1001: Screw_Terminal_01x04, Connector_Phoenix_MC_HighVoltage:PhoenixContact_MCV_1,5_4-G-5.08_1x04_P5.08mm_Vertical, F.Cu at (54.8, -140.4)
- added J1002: Screw_Terminal_01x04, Connector_Phoenix_MC_HighVoltage:PhoenixContact_MCV_1,5_4-G-5.08_1x04_P5.08mm_Vertical, F.Cu at (54.8, -131.1)
- added J1101: Screw_Terminal_01x04, Connector_Phoenix_MC_HighVoltage:PhoenixContact_MCV_1,5_4-G-5.08_1x04_P5.08mm_Vertical, F.Cu at (54.8, -160.4)
- added J1102: Screw_Terminal_01x04, Connector_Phoenix_MC_HighVoltage:PhoenixContact_MCV_1,5_4-G-5.08_1x04_P5.08mm_Vertical, F.Cu at (54.8, -169.7)
- added J1201: Screw_Terminal_01x04, Connector_Phoenix_MC_HighVoltage:PhoenixContact_MCV_1,5_4-G-5.08_1x04_P5.08mm_Vertical, F.Cu at (4.99, -140.4)
- added J1202: Screw_Terminal_01x04, Connector_Phoenix_MC_HighVoltage:PhoenixContact_MCV_1,5_4-G-5.08_1x04_P5.08mm_Vertical, F.Cu at (4.99, -131.1)
- added J1301: Screw_Terminal_01x04, Connector_Phoenix_MC_HighVoltage:PhoenixContact_MCV_1,5_4-G-5.08_1x04_P5.08mm_Vertical, F.Cu at (154.4, -169.7)
- added J1302: Screw_Terminal_01x04, Connector_Phoenix_MC_HighVoltage:PhoenixContact_MCV_1,5_4-G-5.08_1x04_P5.08mm_Vertical, F.Cu at (154.4, -160.4)
- added J1401: Screw_Terminal_01x04, Connector_Phoenix_MC_HighVoltage:PhoenixContact_MCV_1,5_4-G-5.08_1x04_P5.08mm_Vertical, F.Cu at (4.99, -72.4)
- added J1402: Screw_Terminal_01x04, Connector_Phoenix_MC_HighVoltage:PhoenixContact_MCV_1,5_4-G-5.08_1x04_P5.08mm_Vertical, F.Cu at (4.99, -81.7)
- added J1501: Screw_Terminal_01x04, Connector_Phoenix_MC_HighVoltage:PhoenixContact_MCV_1,5_4-G-5.08_1x04_P5.08mm_Vertical, F.Cu at (54.8, -101.7)
- added J1502: Screw_Terminal_01x04, Connector_Phoenix_MC_HighVoltage:PhoenixContact_MCV_1,5_4-G-5.08_1x04_P5.08mm_Vertical, F.Cu at (54.8, -111.1)
- added J1601: Screw_Terminal_01x04, Connector_Phoenix_MC_HighVoltage:PhoenixContact_MCV_1,5_4-G-5.08_1x04_P5.08mm_Vertical, F.Cu at (104.6, -81.7)
- added J1602: Screw_Terminal_01x04, Connector_Phoenix_MC_HighVoltage:PhoenixContact_MCV_1,5_4-G-5.08_1x04_P5.08mm_Vertical, F.Cu at (104.6, -72.4)
- added J1701: Screw_Terminal_01x04, Connector_Phoenix_MC_HighVoltage:PhoenixContact_MCV_1,5_4-G-5.08_1x04_P5.08mm_Vertical, F.Cu at (4.99, -169.7)
- added J1702: Screw_Terminal_01x04, Connector_Phoenix_MC_HighVoltage:PhoenixContact_MCV_1,5_4-G-5.08_1x04_P5.08mm_Vertical, F.Cu at (4.99, -160.4)
- added J1801: Screw_Terminal_01x04, Connector_Phoenix_MC_HighVoltage:PhoenixContact_MCV_1,5_4-G-5.08_1x04_P5.08mm_Vertical, F.Cu at (4.99, -111.1)
- added J1802: Screw_Terminal_01x04, Connector_Phoenix_MC_HighVoltage:PhoenixContact_MCV_1,5_4-G-5.08_1x04_P5.08mm_Vertical, F.Cu at (4.99, -101.7)
- added J1901: Screw_Terminal_01x04, Connector_Phoenix_MC_HighVoltage:PhoenixContact_MCV_1,5_4-G-5.08_1x04_P5.08mm_Vertical, F.Cu at (54.8, -81.7)
- added J1902: Screw_Terminal_01x04, Connector_Phoenix_MC_HighVoltage:PhoenixContact_MCV_1,5_4-G-5.08_1x04_P5.08mm_Vertical, F.Cu at (54.8, -72.4)
- added J301: Screw_Terminal_01x04, Connector_Phoenix_MC_HighVoltage:PhoenixContact_MCV_1,5_4-G-5.08_1x04_P5.08mm_Vertical, F.Cu at (204.2, -169.7)
- added J302: Screw_Terminal_01x04, Connector_Phoenix_MC_HighVoltage:PhoenixContact_MCV_1,5_4-G-5.08_1x04_P5.08mm_Vertical, F.Cu at (204.2, -160.4)
- added J401: Screw_Terminal_01x04, Connector_Phoenix_MC_HighVoltage:PhoenixContact_MCV_1,5_4-G-5.08_1x04_P5.08mm_Vertical, F.Cu at (154.4, -101.7)
- added J402: Screw_Terminal_01x04, Connector_Phoenix_MC_HighVoltage:PhoenixContact_MCV_1,5_4-G-5.08_1x04_P5.08mm_Vertical, F.Cu at (154.4, -111.1)
- added J601: Screw_Terminal_01x04, Connector_Phoenix_MC_HighVoltage:PhoenixContact_MCV_1,5_4-G-5.08_1x04_P5.08mm_Vertical, F.Cu at (154.4, -131.1)
- added J602: Screw_Terminal_01x04, Connector_Phoenix_MC_HighVoltage:PhoenixContact_MCV_1,5_4-G-5.08_1x04_P5.08mm_Vertical, F.Cu at (154.4, -140.4)
- added J701: Screw_Terminal_01x04, Connector_Phoenix_MC_HighVoltage:PhoenixContact_MCV_1,5_4-G-5.08_1x04_P5.08mm_Vertical, F.Cu at (104.6, -111.1)
- added J702: Screw_Terminal_01x04, Connector_Phoenix_MC_HighVoltage:PhoenixContact_MCV_1,5_4-G-5.08_1x04_P5.08mm_Vertical, F.Cu at (104.6, -101.7)
- added J801: Screw_Terminal_01x04, Connector_Phoenix_MC_HighVoltage:PhoenixContact_MCV_1,5_4-G-5.08_1x04_P5.08mm_Vertical, F.Cu at (104.6, -131.1)
- added J802: Screw_Terminal_01x04, Connector_Phoenix_MC_HighVoltage:PhoenixContact_MCV_1,5_4-G-5.08_1x04_P5.08mm_Vertical, F.Cu at (104.6, -140.4)
- added J901: Screw_Terminal_01x04, Connector_Phoenix_MC_HighVoltage:PhoenixContact_MCV_1,5_4-G-5.08_1x04_P5.08mm_Vertical, F.Cu at (104.6, -160.4)
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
